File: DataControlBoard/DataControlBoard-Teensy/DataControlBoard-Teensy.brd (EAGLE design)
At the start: 66 x 88.9 mm, 67 parts, among them IC1 74LS165D, IC2 74LS165D, IC3 74AHC1G04DCK, J1 RS-Interface, J10 Magnet RPi, J11 Boom Cam RPi, J2 Pwr-Conn, J3 Antenna SPI, J9 Static RPi, U1 MAX3232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

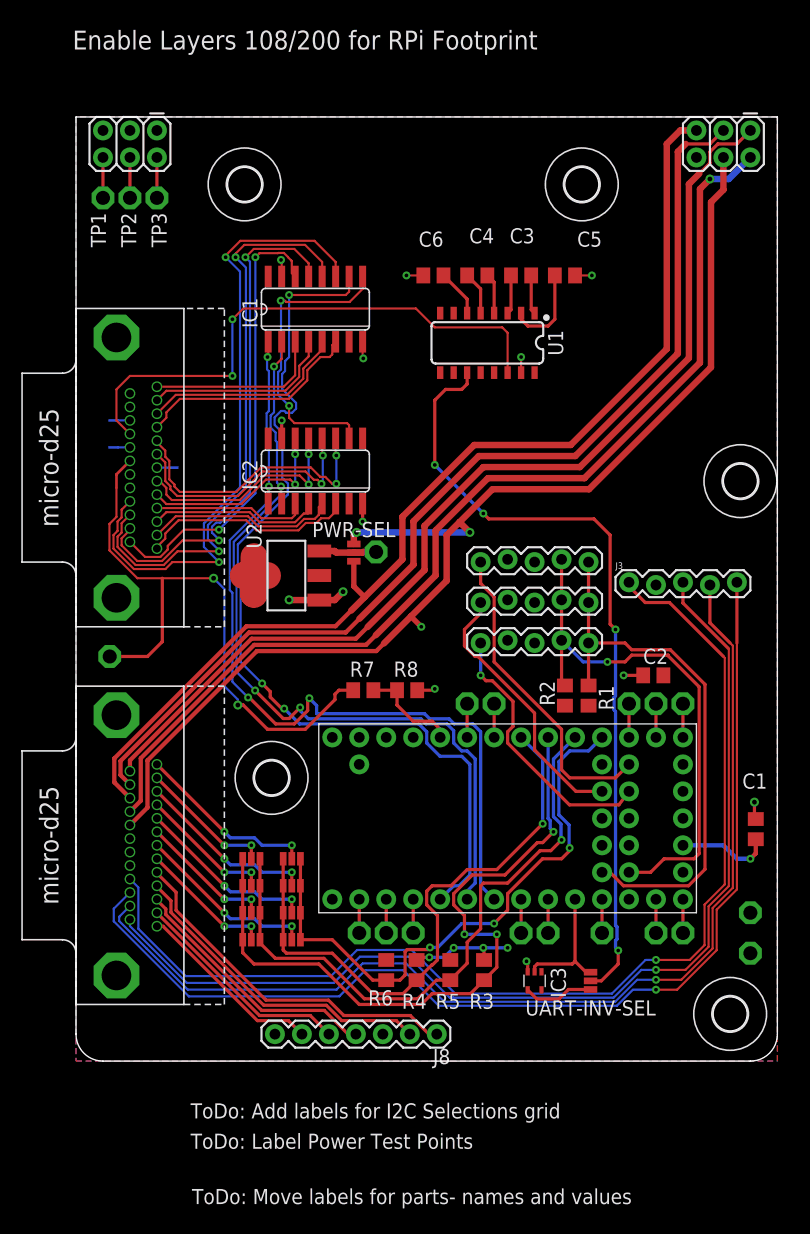
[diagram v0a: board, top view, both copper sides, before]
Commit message: Teensy board ready for double check
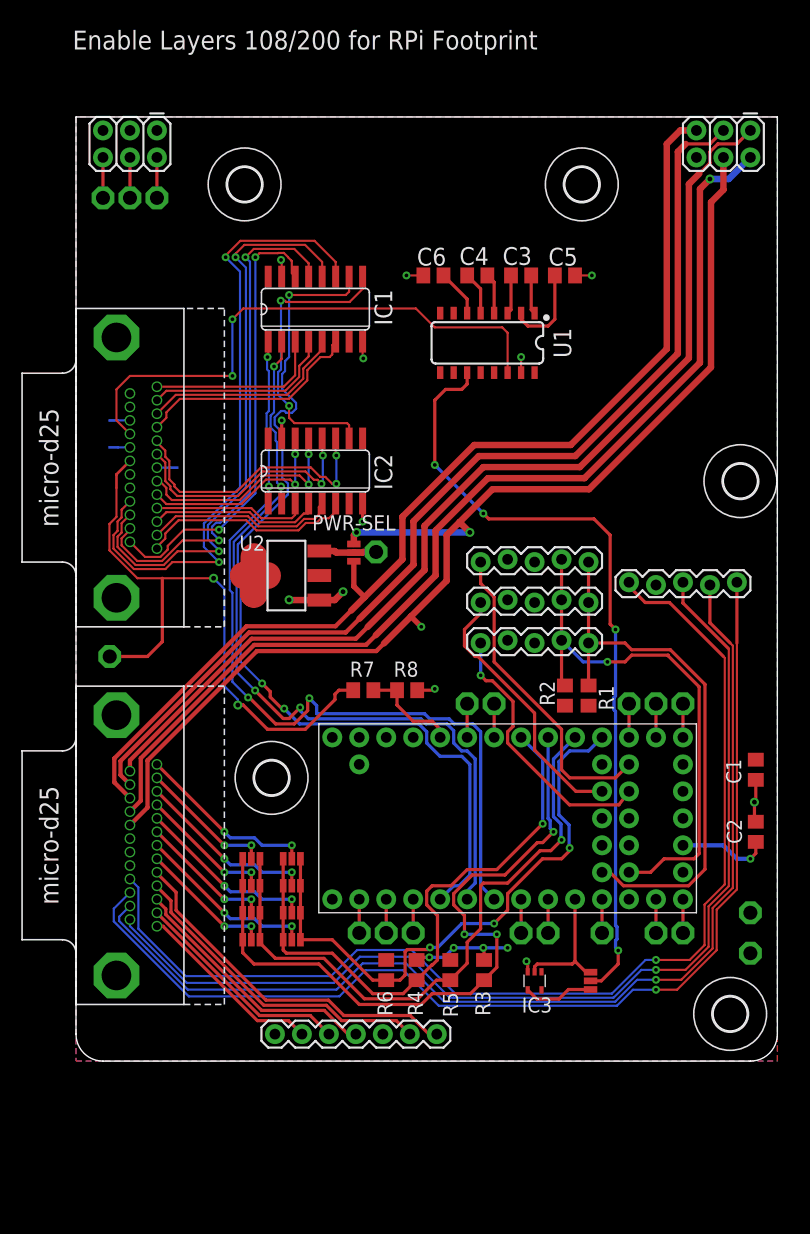
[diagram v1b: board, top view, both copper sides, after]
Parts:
- moved C2 17.6 mm to (64.0, 21.6), turned to 90 degrees
- moved C1 5.59 mm to (64.0, 27.4), turned to 270 degrees
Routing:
- net GND: track 22.8 -> 23.4 mm, vias 13 -> 12
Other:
- board text added: "0 1"
- board text added: "1 2 3"
- board text added: "17 -SS 3V3-NC 10 -MOSI 9 -MISO 11 -SCK"
- board text added: "2 -SDA 3 -SCL 4 -NC GND-NC 17 -En"
- board text added: "3.3V"
- board text added: "5v"
- board text added: "Boom Magnet Static Laser"
- board text added: "BoomCam Magnet Static"
- board text added: "Data Control Board (Teensy) Mines RockSat-X 2019 Mark Gilliland, Graham Braly"
- board text added: "GND"
- board text added: "LSR MAG"
- board text added: "Norm Invrt"
- board text added: "Power Board I/F"
- board text added: "Power Source Select"
- board text added: "REV 1.0"
- board text added: "RS232 Polarity"
- board text added: "RockSat Data I/F"
- board text added: "SDA SCL"
- board text added: "Strobe"
- board text added: "x3"
- board text removed: "ToDo: Add labels for I2C Selections grid"
- board text removed: "ToDo: Label Power Test Points"
- board text removed: "ToDo: Move labels for parts- names and values"

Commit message: Added files neccessary to manufacture
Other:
- board text removed: "Enable Layers 108/200 for RPi Footprint"
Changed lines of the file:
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@@
 <vertex x="66.04" y="88.9"/>
 </polygon>
-<text x="-0.3175" y="95.25" size="1.778" layer="21">Enable Layers 108/200 for RPi Footprint</text>
 <wire x1="66.04" y1="50.8" x2="74.6125" y2="50.8" width="0.2032" layer="108"/>
 <text x="70.1675" y="51.435" size="1.4224" layer="108" font="vector">RPi</text>
@@
 <wire x1="26.72899375" y1="9.82894375" x2="31.337125" y2="9.82894375" width="0.2032" layer="16"/>
 <wire x1="31.337125" y1="9.82894375" x2="31.7090875" y2="9.45698125" width="0.2032" layer="16"/>
-<wire x1="35.197075" y1="5.969" x2="35.1880375" y2="5.9780375" width="0.2032" layer="16"/>
 <wire x1="35.1880375" y1="5.9780375" x2="31.70909375" y2="9.45698125" width="0.2032" layer="16"/>
 <wire x1="59.563" y1="14.574175" x2="61.468" y2="16.479175" width="0.2032" layer="1"/>

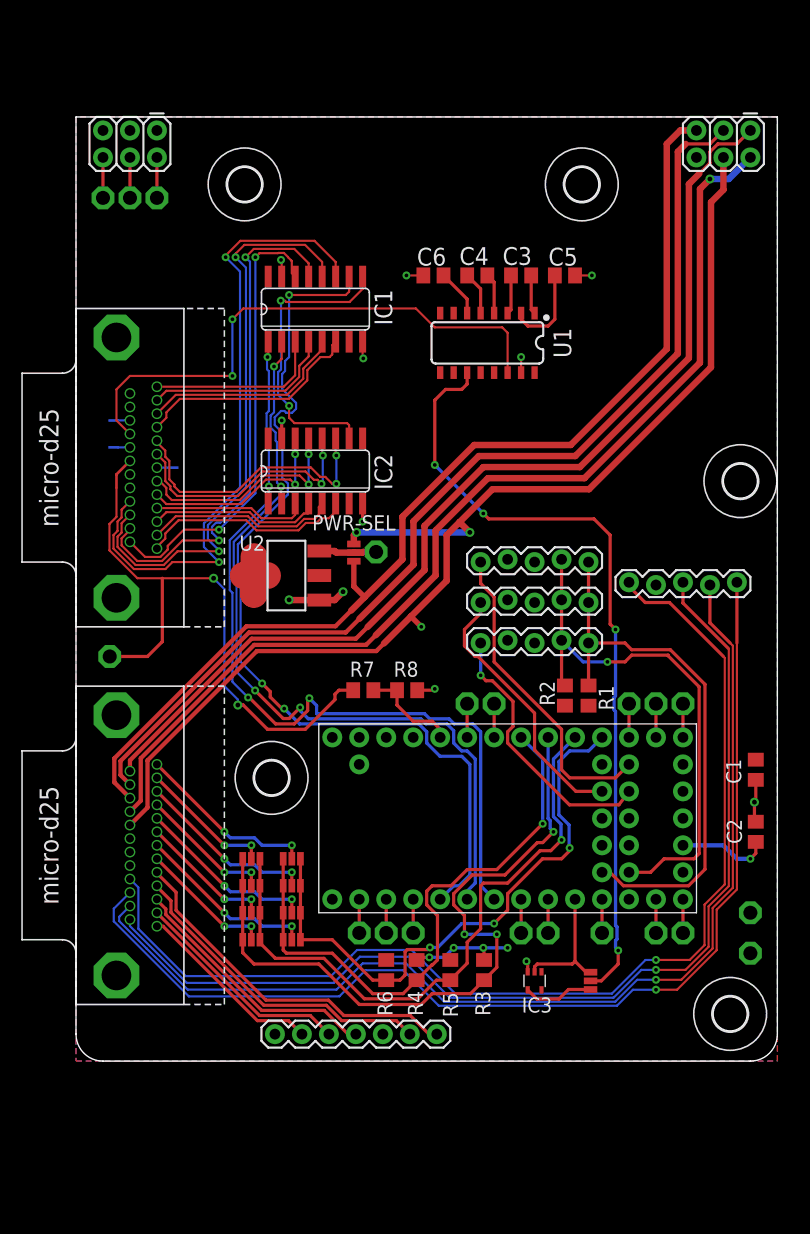
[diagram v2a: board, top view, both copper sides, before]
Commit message: Added rev2 , including Teensy supply voltage and other minor issues.
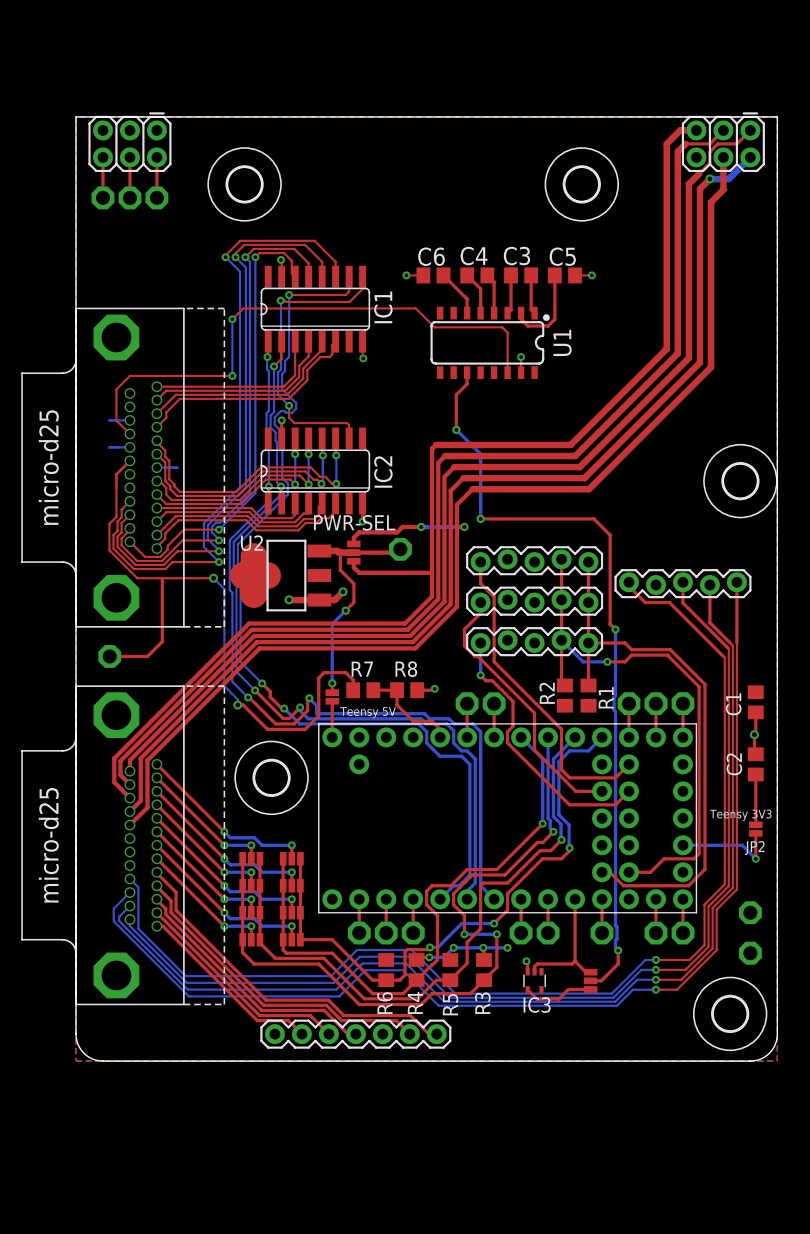
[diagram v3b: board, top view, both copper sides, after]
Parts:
- added JP1, JP2: JUMPER-SMT_2_NO_NO-SILK, SparkFun-Jumpers:SMT-JUMPER_2_NO_NO-SILK
- moved C2 6.35 mm to (64.0, 27.9)
- moved C1 6.35 mm to (64.0, 33.8)
- moved TP5 2.30 mm to (30.5, 48.2)
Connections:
- removed net +3.3V: TP6.TP
- removed net VIN: B1.VIN
- new net 3V3-JUMPERED: B1.3.3V, JP2.2
- new net 5V-JUMPERED: B1.VIN, JP1.2
- net +3V3: now also JP2.1, TP6.TP; no longer B1.3.3V
- net +5V: now also JP1.1
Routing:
- net +5V: track 5.44 -> 22.4 mm, vias 0 -> 2
- net 5V-DIG-MAG: track 101.1 -> 111.3 mm
- net 3V3-JUMPERED: track 0.00 -> 9.77 mm, vias 0 -> 1
- net 5V-DIG-CAM: track 97.5 -> 102.6 mm
- net 5V-DIG-TX: track 96.7 -> 101.1 mm
- net +3V3: track 25.1 -> 21.1 mm, vias 5 -> 4
- net 5V-DIG-STA: track 98.3 -> 102.1 mm
- net PDB-STROBE: track 58.1 -> 61.8 mm
- net 5V-JUMPERED: track 0.00 -> 3.40 mm
- net N$20: track 74.3 -> 72.2 mm
- net 5V-DIG-LASER: track 112.5 -> 113.2 mm, vias 3 -> 2
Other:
- board text added: "Teensy 3V3"
- board text added: "Teensy 5V"

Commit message: Moved some files around. Made progress on power management board
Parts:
- moved J6 7.62 mm to (63.5, 80.0)
- moved J7 7.62 mm to (7.62, 80.0)
- moved TP1 6.35 mm to (2.54, 74.9)
- moved TP2 6.35 mm to (5.08, 74.9)
- moved TP3 6.35 mm to (7.62, 74.9)
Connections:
- new net ANT-BUSY: J3.2
- new net CAM-USB_N: J2.P19
- new net CAM-USB_P: J2.P18
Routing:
- net 5V-DIG-TX: track 101.1 -> 93.5 mm
- net 5V-DIG-STA: track 102.1 -> 94.5 mm
- net 5V-DIG-MAG: track 111.3 -> 103.7 mm
- net 5V-DIG-LASER: track 113.2 -> 105.5 mm
- net 5V-DIG-CAM: track 102.6 -> 95.0 mm
- net N$6: track 3.81 -> 2.54 mm
- net N$28: track 3.81 -> 2.54 mm
- net N$27: track 3.81 -> 2.54 mm
- net ANT-SS: track 104.8 -> 103.7 mm
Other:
- board text added: "17 -SS 24 -BUSY 10 -MOSI 9 -MISO 11 -SCK"
- board text added: "REV 2.0"
- board text removed: "17 -SS 3V3-NC 10 -MOSI 9 -MISO 11 -SCK"
- board text removed: "REV 1.0"

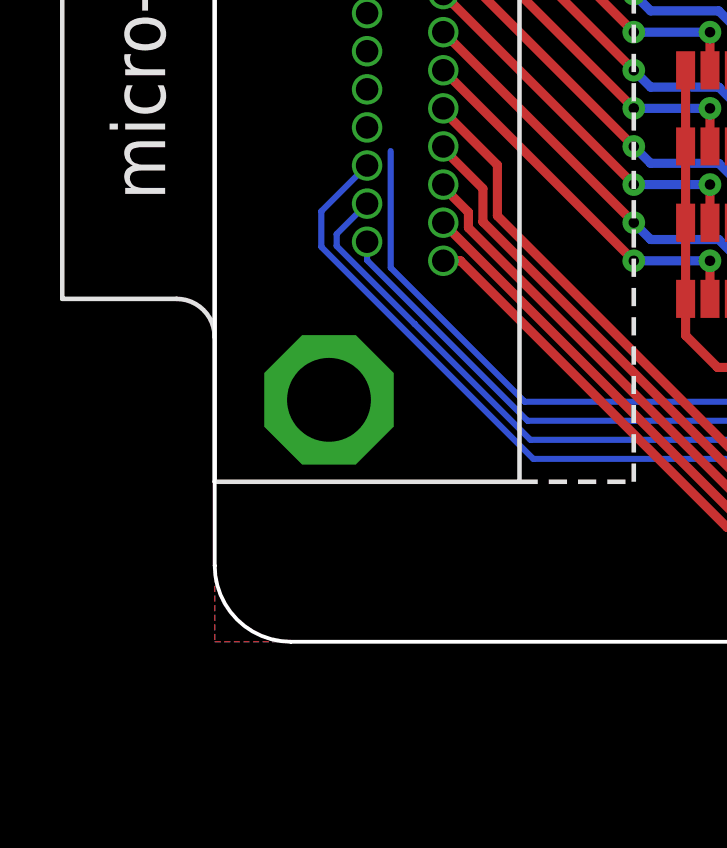
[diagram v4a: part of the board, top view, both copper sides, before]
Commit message: Implemented ANT-BUSY signal to replace 5V supply on lidar
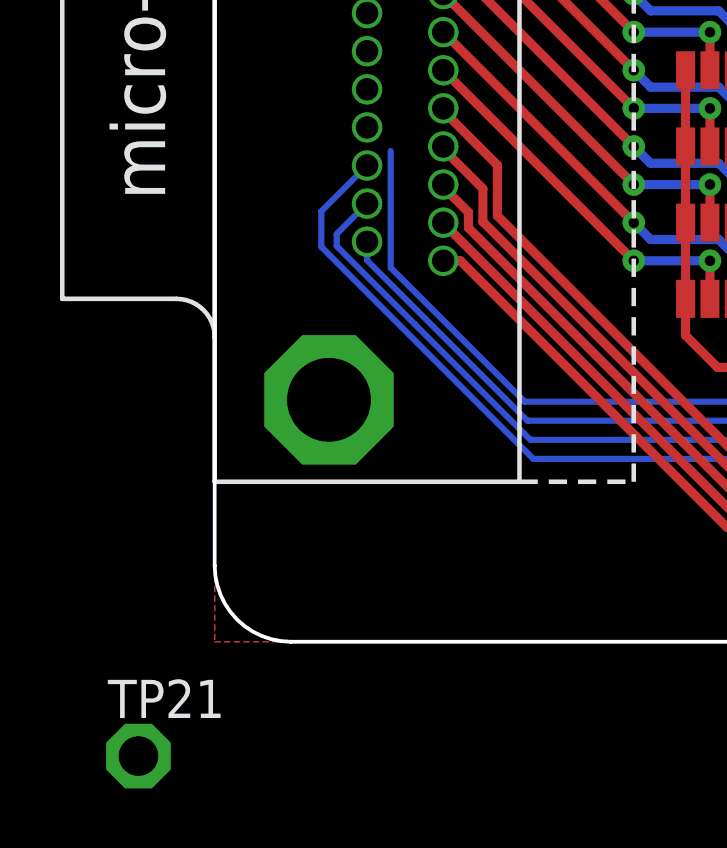
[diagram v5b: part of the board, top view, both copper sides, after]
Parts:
- added TP21: TPPAD1-13, testpad:P1-13
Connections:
- net ANT-BUSY: now also J2.P3
- net LASER-VS-1: now also TP21.TP; no longer J2.P3
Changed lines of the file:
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@@
 <attribute name="VALUE" x="62.865" y="21.844" size="0.6096" layer="27" font="vector" ratio="20" rot="R270" align="top-center"/>
+</element>
+<element name="TP21" library="testpad" library_urn="urn:adsk.eagle:library:385" package="P1-13" package3d_urn="urn:adsk.eagle:package:27946/1" value="TPPAD1-13" x="-2.54" y="-3.81" smashed="yes">
+<attribute name="NAME" x="-3.556" y="-2.54" size="1.27" layer="25" ratio="10"/>
+<attribute name="POPULARITY" value="12" x="-2.54" y="-3.81" size="1.778" layer="27" display="off"/>
+<attribute name="TP_SIGNAL_NAME" value="" x="-2.54" y="-3.81" size="1.778" layer="27" display="off"/>
+<attribute name="VALUE" x="-2.54" y="-3.81" size="0.0254" layer="27"/>
 </element>
 </elements>
@@
 <signal name="LASER-VS-1">
 <contactref element="J8" pad="4"/>
-<contactref element="J2" pad="P3"/>
 <wire x1="26.3525" y1="2.54" x2="25.60855625" y2="2.54" width="0.3048" layer="1"/>
 <wire x1="25.60855625" y1="2.54" x2="23.37335625" y2="4.7752" width="0.3048" layer="1"/>
 <wire x1="23.37335625" y1="4.7752" x2="17.4818" y2="4.7752" width="0.3048" layer="1"/>
 <wire x1="8.4582" y1="13.7988" x2="8.4582" y2="14.3172" width="0.3048" layer="1"/>
-<wire x1="7.62" y1="15.1554" x2="7.62" y2="15.24" width="0.3048" layer="1"/>
 <wire x1="8.4582" y1="14.3172" x2="7.62" y2="15.1554" width="0.3048" layer="1"/>
 <wire x1="17.4818" y1="4.7752" x2="8.4582" y2="13.7988" width="0.3048" layer="1"/>
+<contactref element="TP21" pad="TP"/>
+<wire x1="-2.54" y1="-3.81" x2="8.4582" y2="13.7988" width="0" layer="19" extent="1-1"/>
 </signal>
 <signal name="LASER-DTR">
@@
 <signal name="ANT-BUSY">
 <contactref element="J3" pad="2"/>
+<contactref element="J2" pad="P3"/>
+<wire x1="7.62" y1="15.24" x2="54.61" y2="44.831" width="0" layer="19" extent="1-1"/>
 </signal>
 <signal name="CAM-USB_P">

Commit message: Routed data control board
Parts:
- added TP22, TP23: TPPAD1-13, testpad:P1-13
- moved TP21 17.7 mm to (14.0, 2.54)
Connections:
- net CAM-USB_N: now also TP23.TP
- net CAM-USB_P: now also TP22.TP
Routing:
- net ANT-BUSY: track 0.00 -> 98.1 mm, vias 0 -> 1
- net CAM-USB_P: track 0.00 -> 55.6 mm, vias 0 -> 1
- net CAM-USB_N: track 0.00 -> 55.5 mm, vias 0 -> 1
- net LASER-VS-1: track 24.3 -> 13.6 mm
- net ANT-SS: track 103.7 -> 99.9 mm
- net ANT-MOSI: track 98.8 -> 96.7 mm
- net ANT-MISO: track 100.9 -> 99.0 mm
- net ANT-SCK: track 103.0 -> 101.7 mm
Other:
- board text added: "LIDAR 5V"
- board text added: "N"
- board text added: "P"
- board text added: "USB"
